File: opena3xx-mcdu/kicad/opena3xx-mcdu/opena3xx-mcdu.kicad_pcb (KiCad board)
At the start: 2 copper layers, 148 x 225 mm, 145 parts, among them J1 Conn_02x01, J2 Conn_02x01, J3 Conn_02x01, J4 Conn_02x01, J5 Conn_02x01, J6 Conn_02x01, J7 Conn_02x01, SW1 TLL-6A, SW10 TLL-6A, SW100 SW_MEC_5E, SW11 TLL-6A, SW12 TLL-6A, SW13 TLL-6A, SW14 TLL-6A, SW15 TLL-6A, SW16 TLL-6A, SW17 TLL-6A, SW18 TLL-6A, SW19 TLL-6A, SW2 TLL-6A, SW20 TLL-6A, SW21 TLL-6A, SW22 TLL-6A, SW23 TLL-6A, SW24 TLL-6A, SW25 TLL-6A, SW26 TLL-6A, SW27 TLL-6A, SW28 TLL-6A, SW29 TLL-6A, SW3 TLL-6A, SW30 TLL-6A, SW31 TLL-6A, SW32 TLL-6A, SW33 TLL-6A, SW34 TLL-6A, SW35 TLL-6A, SW36 TLL-6A, SW37 TLL-6A, SW38 TLL-6A, SW39 TLL-6A, SW4 TLL-6A, SW40 TLL-6A, SW41 TLL-6A, SW42 TLL-6A, SW43 TLL-6A, SW44 TLL-6A, SW45 TLL-6A, SW46 TLL-6A, SW47 TLL-6A, SW48 TLL-6A, SW49 TLL-6A, SW5 TLL-6A, SW50 TLL-6A, SW51 TLL-6A, SW52 TLL-6A, SW53 TLL-6A, SW54 TLL-6A, SW55 TLL-6A, SW56 TLL-6A, SW57 TLL-6A, SW58 TLL-6A, SW59 TLL-6A, SW6 TLL-6A, SW60 TLL-6A, SW61 TLL-6A, SW62 TLL-6A, SW63 TLL-6A, SW64 TLL-6A, SW65 TLL-6A, SW66 TLL-6A, SW67 TLL-6A, SW68 TLL-6A, SW69 TLL-6A, SW7 TLL-6A, SW70 TLL-6A, SW71 TLL-6A, SW72 TLL-6A, SW8 TLL-6A, SW9 TLL-6A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

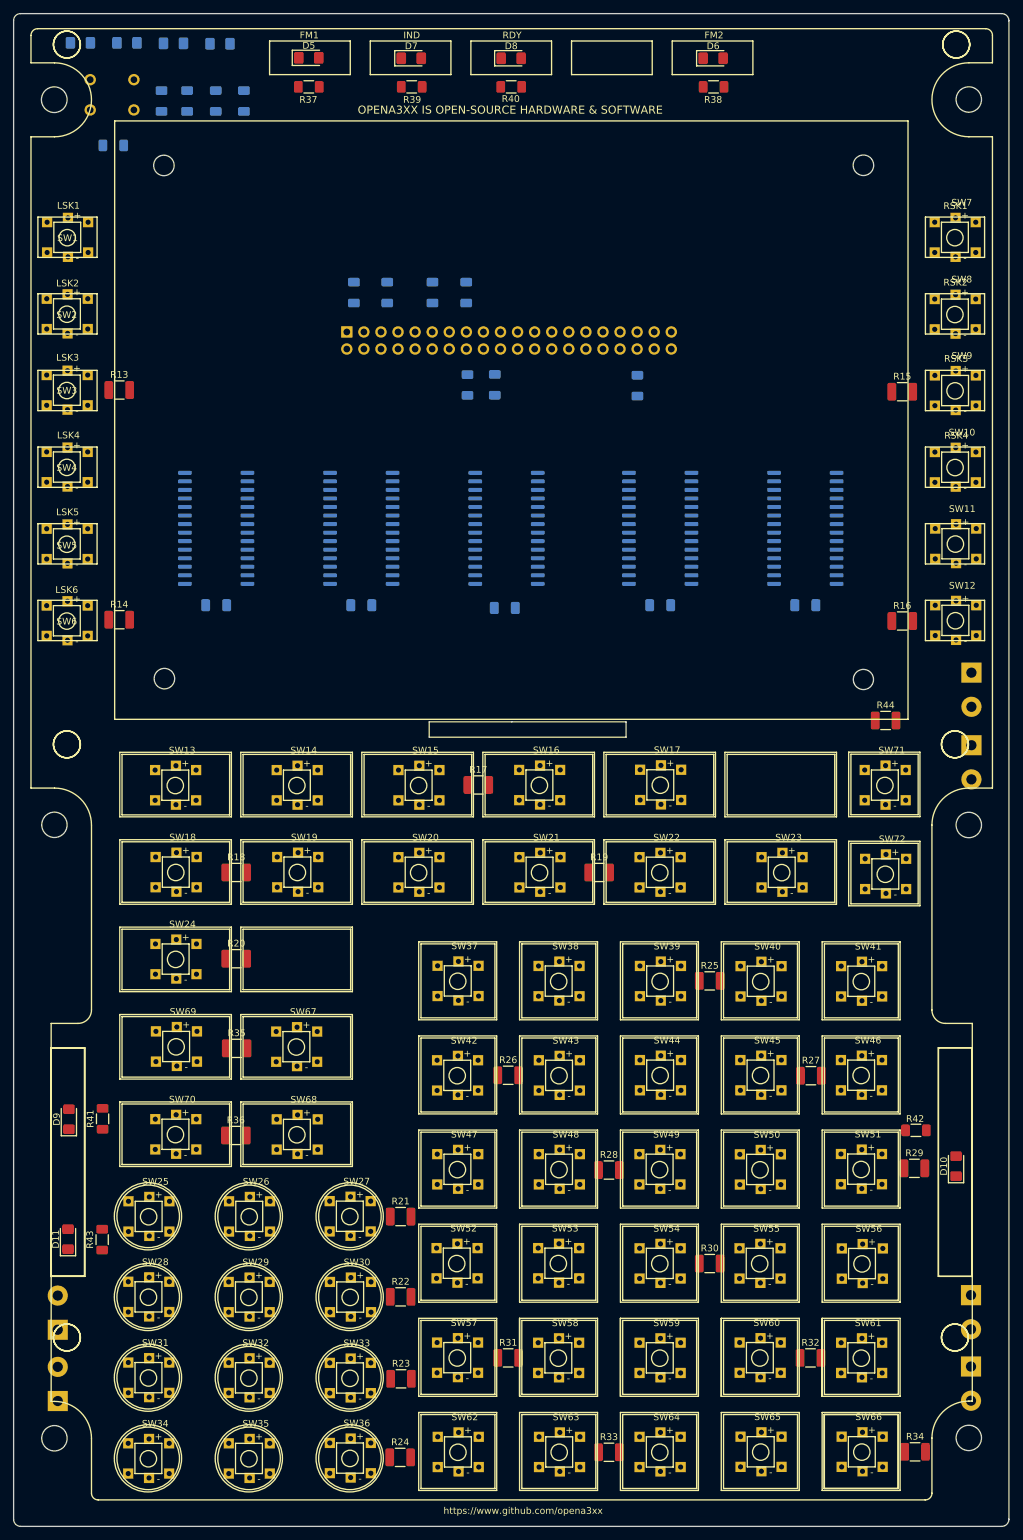
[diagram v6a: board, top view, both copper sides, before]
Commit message: Adding all buttons/led marking as Front Silk
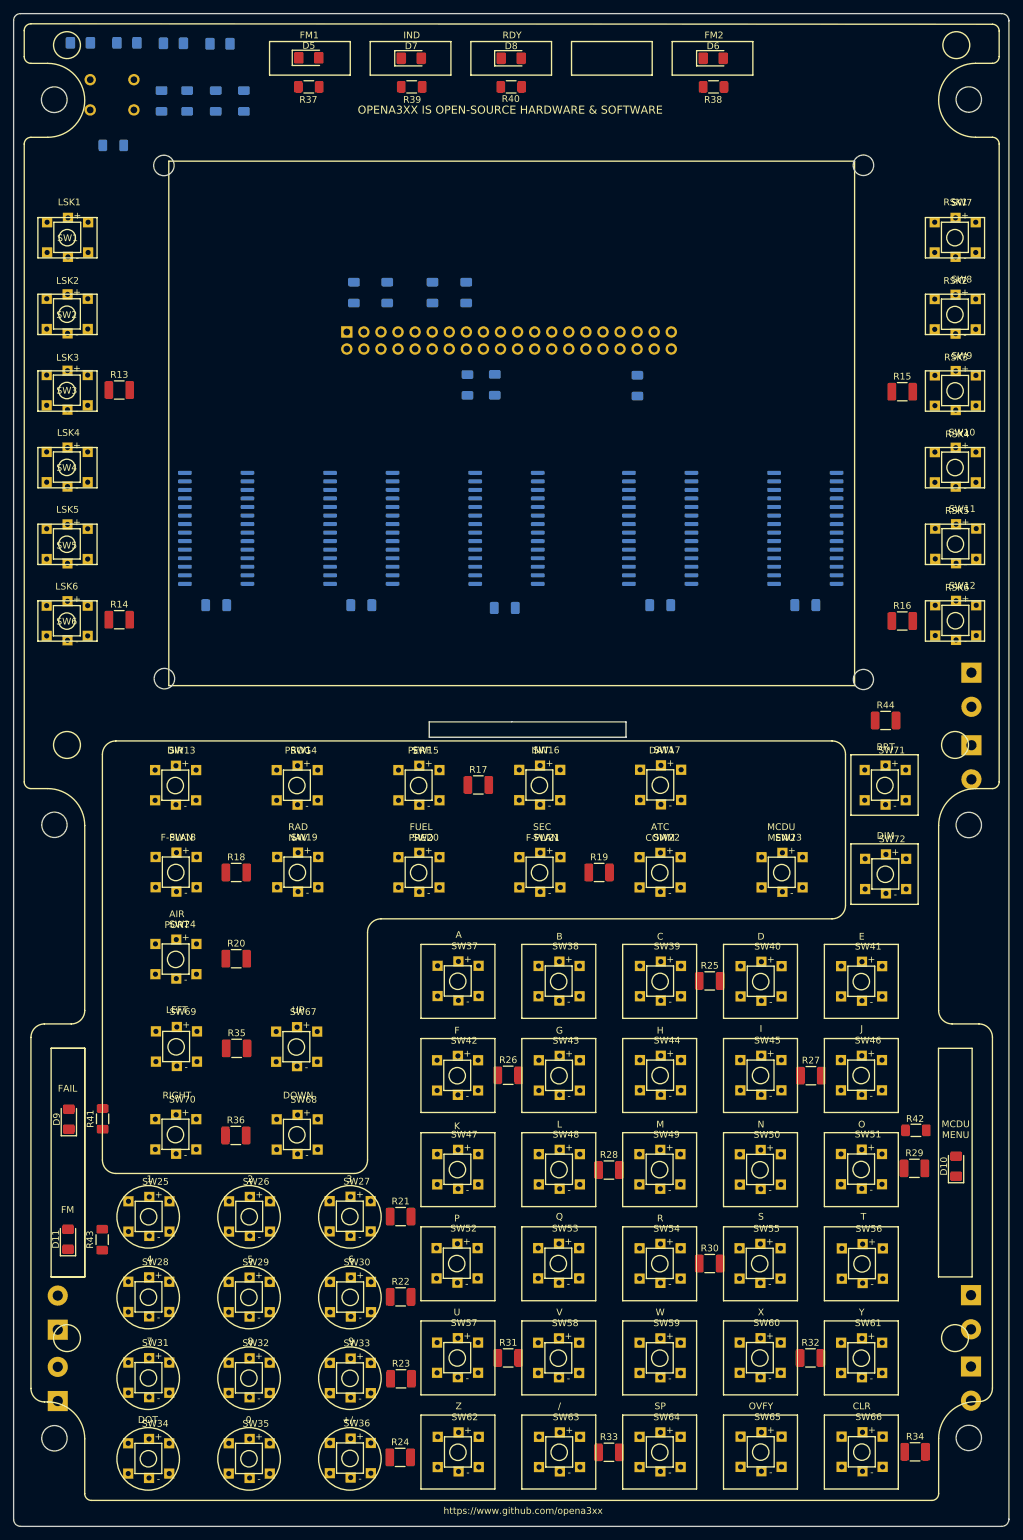
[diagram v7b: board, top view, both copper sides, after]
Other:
- board text added: "+/-"
- board text added: "/"
- board text added: "0"
- board text added: "1"
- board text added: "2"
- board text added: "3"
- board text added: "4"
- board text added: "5"
- board text added: "6"
- board text added: "7"
- board text added: "8"
- board text added: "9"
- board text added: "A"
- board text added: "AIR PORT"
- board text added: "ATC COMM"
- board text added: "B"
- board text added: "BRT"
- board text added: "C"
- board text added: "CLR"
- board text added: "D"
- board text added: "DATA"
- board text added: "DIM"
- board text added: "DIR"
- board text added: "DOT"
- board text added: "DOWN"
- board text added: "E"
- board text added: "F"
- board text added: "F-PLAN"
- board text added: "FAIL"
- board text added: "FM"
- board text added: "FUEL PRED"
- board text added: "G"
- board text added: "H"
- board text added: "I"
- board text added: "INIT"
- board text added: "J"
- board text added: "K"
- board text added: "L"
- board text added: "LEFT"
- board text added: "M"
- board text added: "MCDU MENU"
- board text added: "N"
- board text added: "O"
- board text added: "OVFY"
- board text added: "P"
- board text added: "PERF"
- board text added: "PROG"
- board text added: "Q"
- board text added: "R"
- board text added: "RAD NAV"
- board text added: "RIGHT"
- board text added: "RSK5"
- board text added: "RSK6"
- board text added: "S"
- board text added: "SEC F-PLAN"
- board text added: "SP"
- board text added: "T"
- board text added: "U"
- board text added: "UP"
- board text added: "V"
- board text added: "W"
- board text added: "X"
- board text added: "Y"
- board text added: "Z"

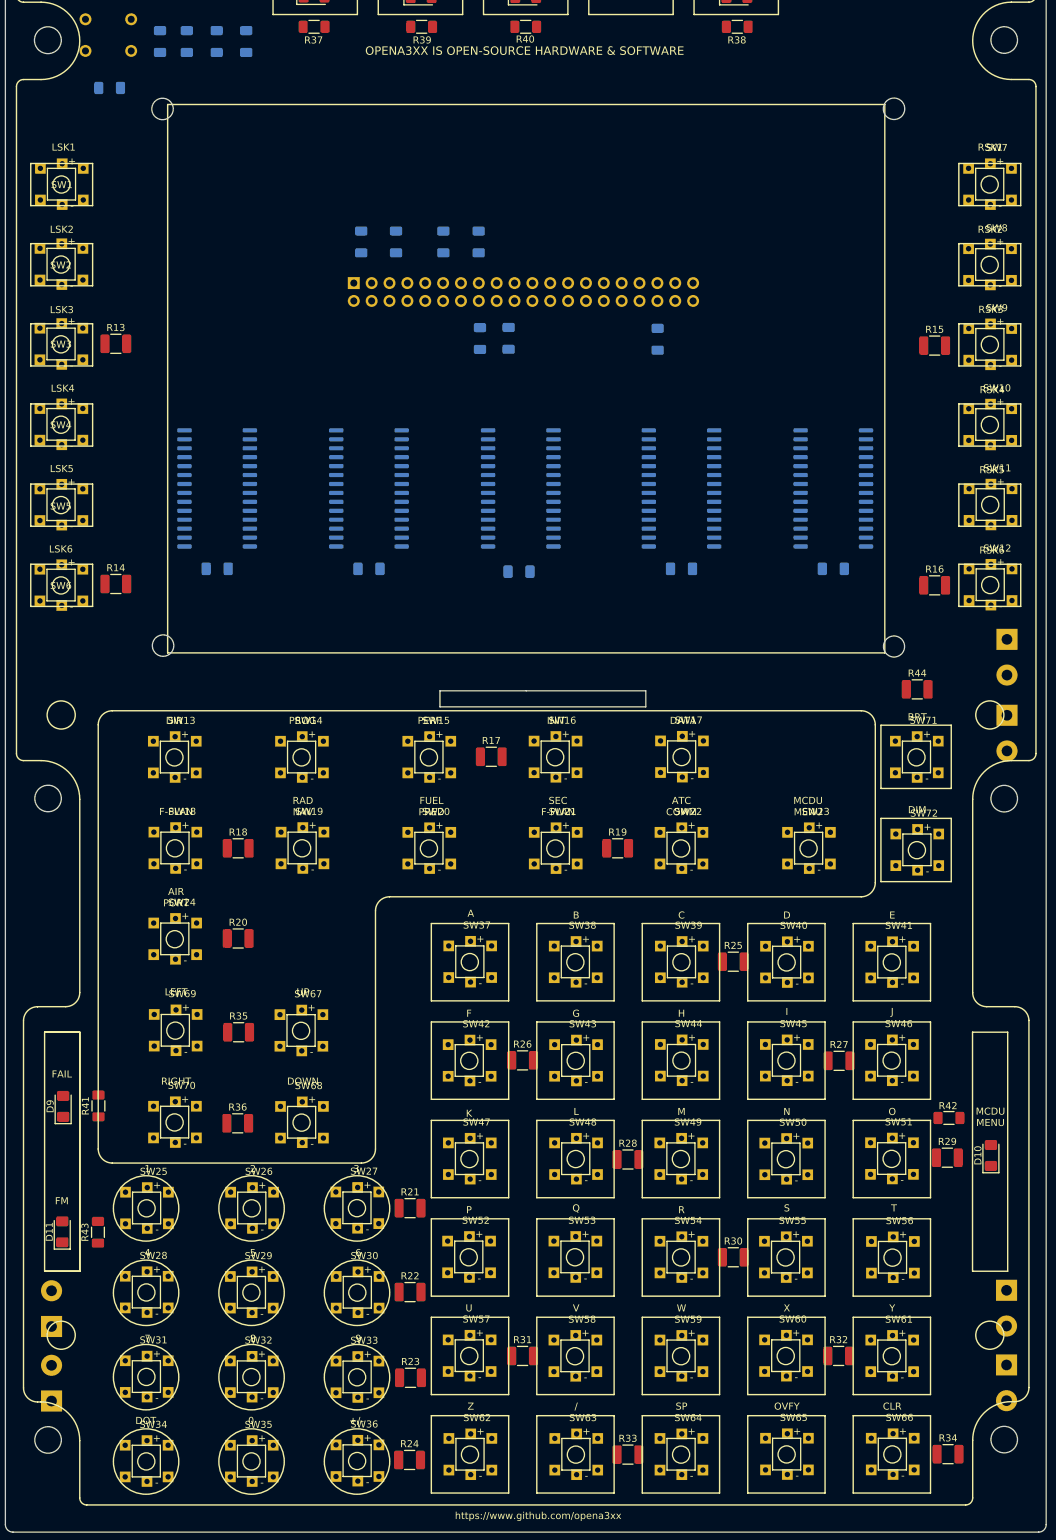
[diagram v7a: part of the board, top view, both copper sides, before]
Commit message: Finished all markings and moved also component reference to the right position.
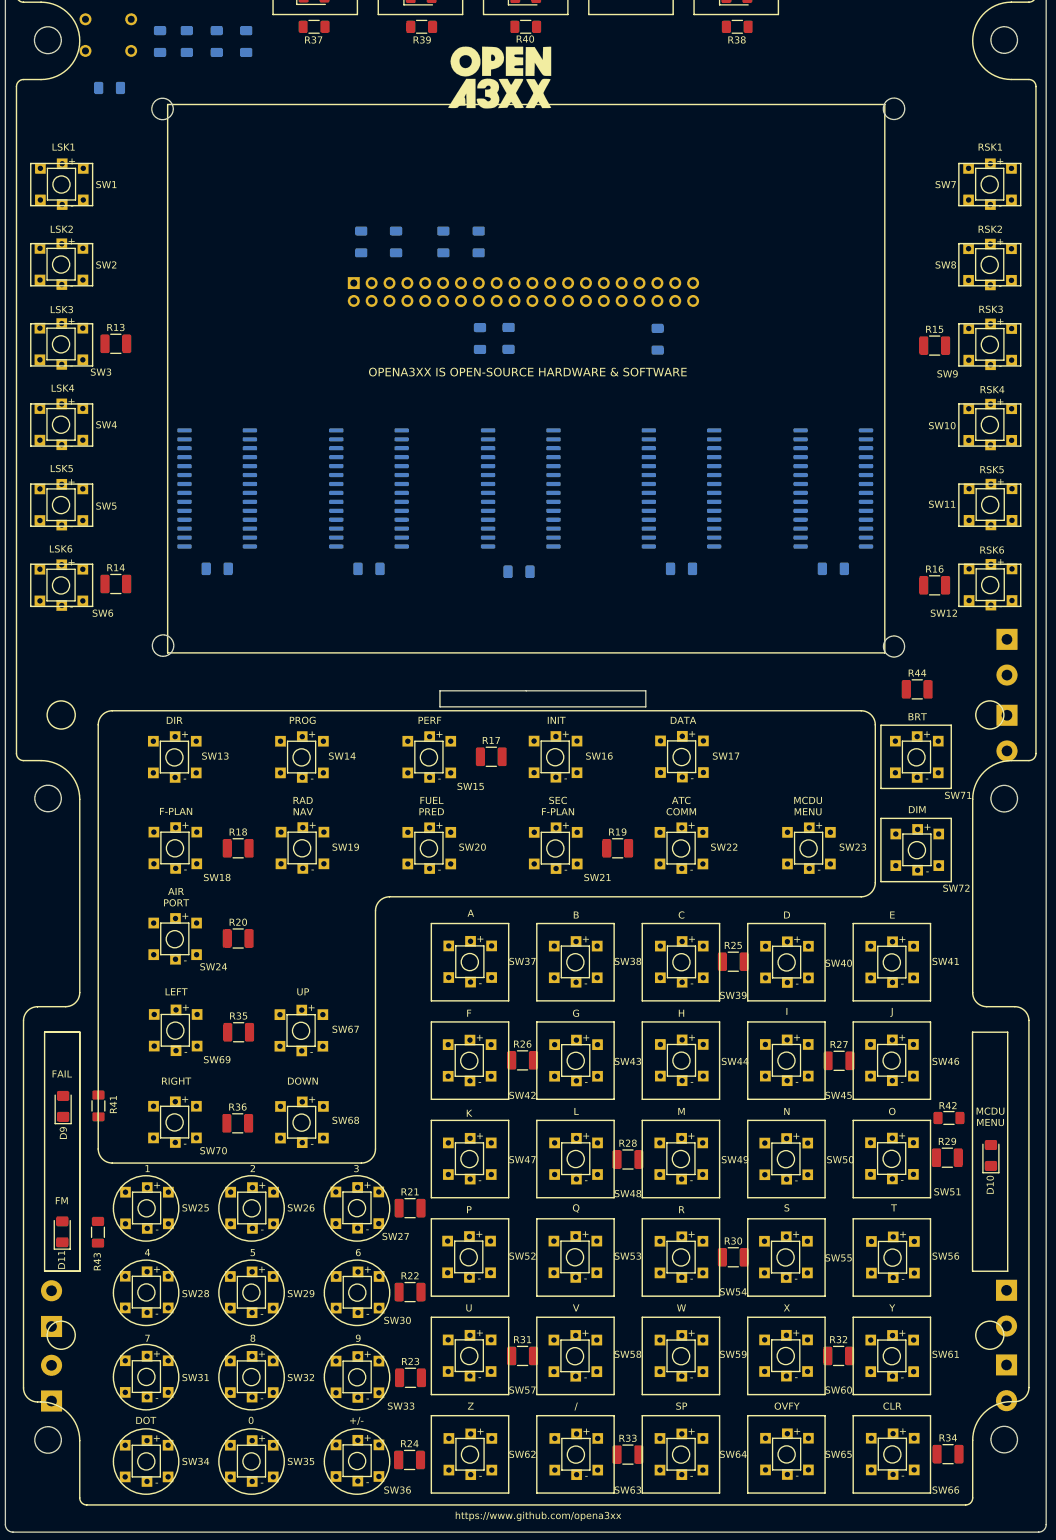
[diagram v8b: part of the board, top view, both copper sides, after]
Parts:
- added G***: LOGO, openaa3xx:logo, F.Cu at (201.5, 45.7)
